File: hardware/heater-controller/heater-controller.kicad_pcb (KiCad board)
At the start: 2 copper layers, 60 x 60 mm, 28 parts, among them J101 PicoLiPo, J201 heater LiPo, J202 heater, J203 heater_SW_EX, J301 Thermistor, Q201 Nch, SW101 Power, SW201 heater_SW

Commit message: kicad編集
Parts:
- C301: footprint Capacitor_SMD:C_0402_1005Metric -> Capacitor_SMD:C_0805_2012Metric
- D102, SW101: value Power -> power
- J101: value PicoLiPo -> pico LiPo
- moved C301 2.06 mm to (144.5, 83.5)
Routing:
- net VDD: track 50.9 -> 60.3 mm, vias 2 -> 0

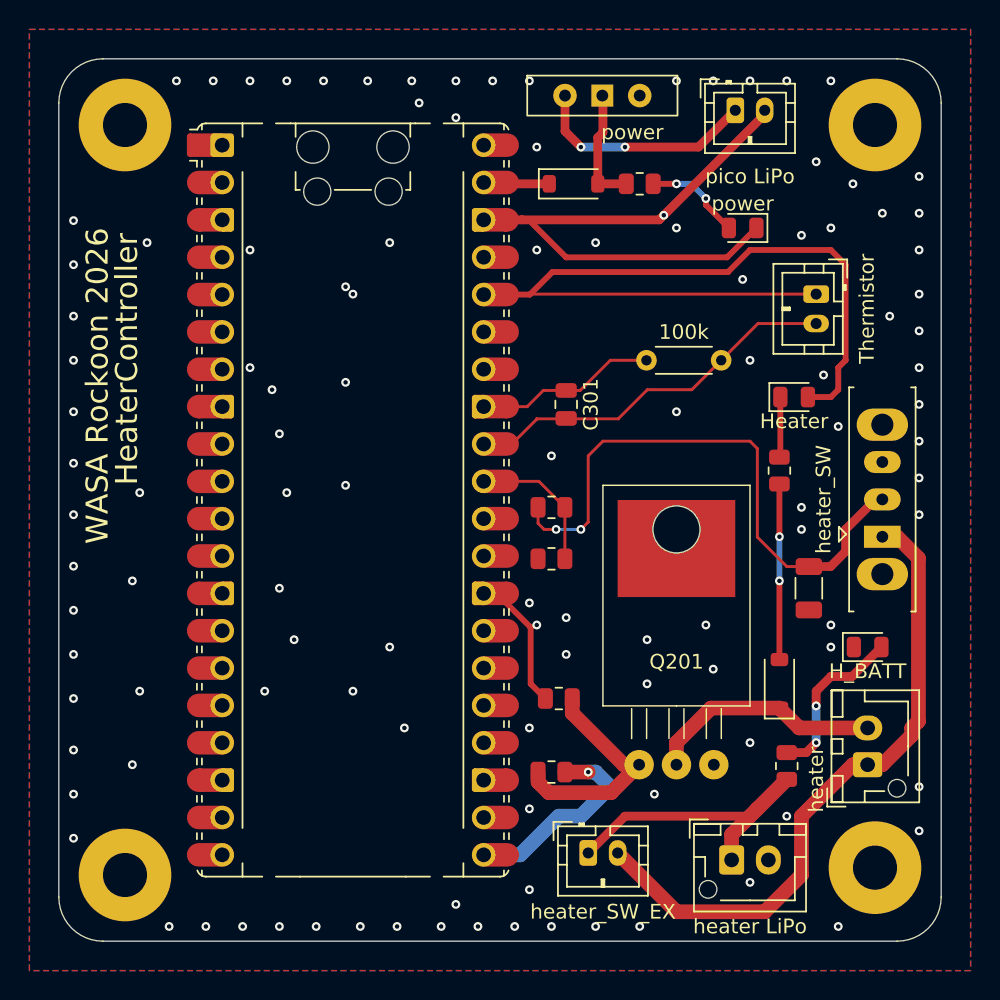
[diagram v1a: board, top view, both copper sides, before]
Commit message: BBMで問題がなければ発注可能
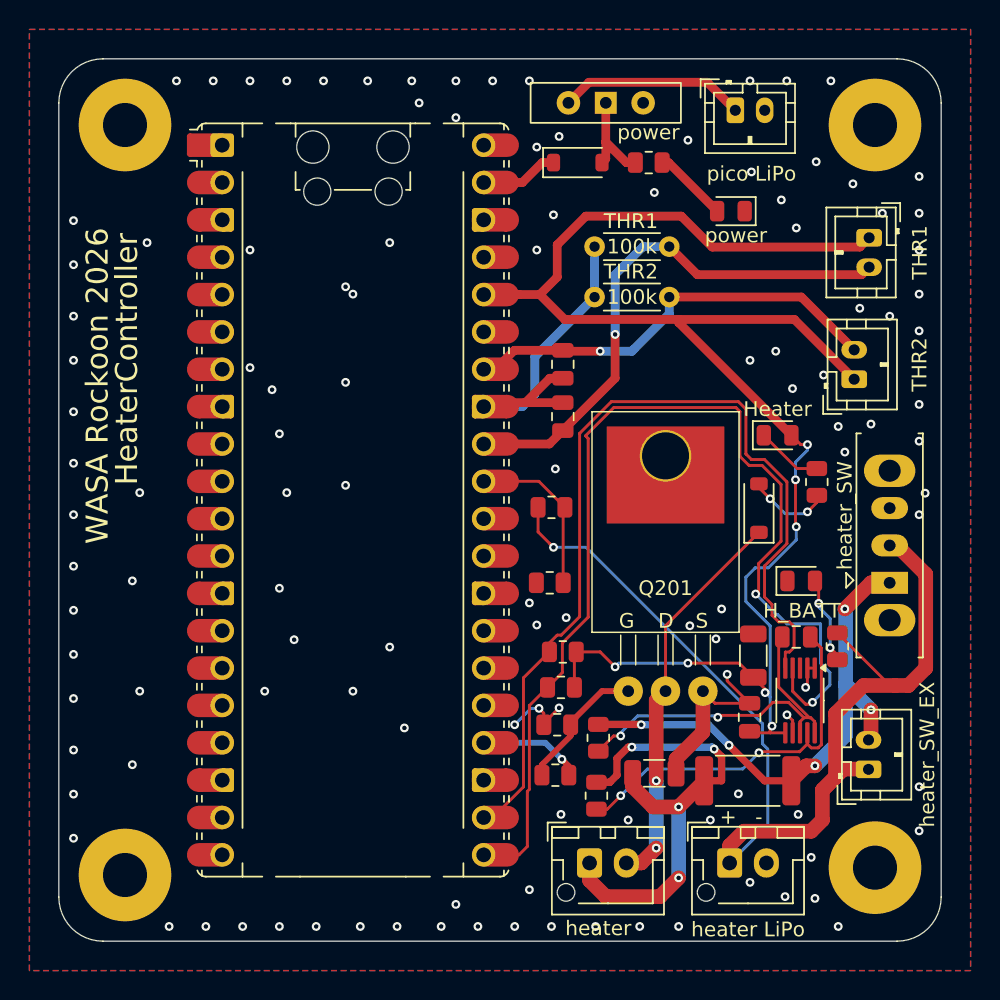
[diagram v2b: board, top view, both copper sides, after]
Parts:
- added C202: 0.1u, Capacitor_SMD:C_0805_2012Metric, F.Cu at (160.1, 99.3)
- added C203: 10uF, Capacitor_SMD:C_1206_3216Metric, F.Cu at (157.2, 100.6)
- added C204: 100nF, Capacitor_SMD:C_0805_2012Metric, F.Cu at (157.0, 104.8)
- added C302: 0.1u, Capacitor_SMD:C_0805_2012Metric, F.Cu at (144.3, 80.8)
- added J302: THR2, Connector_JST:JST_PH_B2B-PH-K_1x02_P2.00mm_Vertical, F.Cu at (164.1, 81.8)
- added R207: 20mΩ, Resistor_SMD:R_2512_6332Metric, F.Cu at (156.8, 109.1)
- added R208: 10k, Resistor_SMD:R_0805_2012Metric, F.Cu at (144.3, 100.3)
- added R209: 10k, Resistor_SMD:R_0805_2012Metric, F.Cu at (144.1, 102.7)
- added R210: 10, Resistor_SMD:R_0805_2012Metric, F.Cu at (146.6, 110.1)
- added R211: 10, Resistor_SMD:R_0805_2012Metric, F.Cu at (146.7, 106.2)
- added R302: 100k, Resistor_THT:R_Axial_DIN0204_L3.6mm_D1.6mm_P5.08mm_Horizontal, F.Cu at (151.5, 76.2)
- added U201: INA226, Package_SO:VSSOP-10_3x3mm_P0.5mm, F.Cu at (160.4, 103.6)
- J301: value Thermistor -> THR1
- R202: value 10k -> 22k
- moved J202 20.1 mm to (146.1, 114.7), turned to 0 degrees
- moved J203 19.9 mm to (165.1, 108.3), turned to 90 degrees
- moved C201 16.4 mm to (150.5, 108.6), turned to 180 degrees
- moved D203 12.0 mm to (157.6, 90.6)
- moved R201 8.84 mm to (162.9, 99.9), turned to 90 degrees
- moved R301 8.50 mm to (151.5, 72.8)
- moved D201 6.38 mm to (160.5, 95.5)
- moved J301 5.26 mm to (165.1, 72.2)
- moved Q201 5.06 mm to (151.3, 103.0)
- moved SW201 3.17 mm to (166.5, 93.1)
- moved D202 2.83 mm to (158.9, 85.6)
- moved R206 2.66 mm to (161.5, 88.8)
- moved R204 1.79 mm to (143.9, 105.3)
- moved R203 1.64 mm to (143.4, 95.6)
- moved R101 1.57 mm to (150.1, 67.1)
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- renumbered A1 to A101
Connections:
- net /Thermistor/AGND renamed /Thermistor1/AGND
- net /Thermistor/R_Thermistor renamed /Thermistor1/R_Thermistor1
- A101 pad 21: /Heater/heater_con -> /Heater/SDA
- A101 pad 22: unconnected-(A1-GPIO17-Pad22) -> /Heater/SCL
- A101 pad 24: unconnected-(A1-GPIO18-Pad24)_1 -> /Heater/heater_con
- A101 pad 34: unconnected-(A1-GPIO28_ADC2-Pad34) -> /Thermistor1/R_Thermistor2
- C201 pad 2: VPP_h -> Net-(J202-Pin_1)
- J203 pad 2: Net-(J202-Pin_1) -> Net-(J203-Pin_2)
- SW201 pad 1: Net-(J202-Pin_1) -> Net-(J203-Pin_2)
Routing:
- net /Heater/SDA: track 0.00 -> 73.0 mm, vias 0 -> 2
- net /Heater/SCL: track 0.00 -> 62.7 mm
- net VDD: track 60.3 -> 108.6 mm, vias 0 -> 7
- net Net-(J203-Pin_2): track 0.00 -> 36.6 mm, vias 0 -> 5
- net /Thermistor1/R_Thermistor2: track 0.00 -> 28.6 mm, vias 0 -> 1
- net GND: track 49.0 -> 20.6 mm, vias 115 -> 121
- net Net-(U201-Vin-): track 0.00 -> 25.7 mm, vias 0 -> 2
- net Net-(U201-Vbus): track 0.00 -> 25.1 mm, vias 0 -> 2
- net VPP_h: track 59.4 -> 74.8 mm, vias 2 -> 1
- net /Thermistor1/AGND: track 12.6 -> 23.5 mm
- net Net-(D203-K): track 16.0 -> 26.8 mm, vias 0 -> 2
- net Net-(J202-Pin_1): track 44.3 -> 33.7 mm, vias 0 -> 4
- net /Thermistor1/R_Thermistor1: track 26.2 -> 36.1 mm, vias 0 -> 1
- net /Heater/heater_con: track 14.0 -> 7.06 mm
- net Net-(Q201-G): track 15.6 -> 9.19 mm
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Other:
- board text added: "+"
- board text added: "-"
- board text added: "THR1"
- board text added: "THR2"
